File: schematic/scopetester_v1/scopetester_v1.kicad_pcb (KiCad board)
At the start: 2 copper layers, 73.7 x 54.4 mm, 42 parts, among them J1 CON_PWR, J2 Conn_01x04, J3 AVR_ISP, SW1 SW_Push, U1 ATmega8A-P, Y1 16MHz

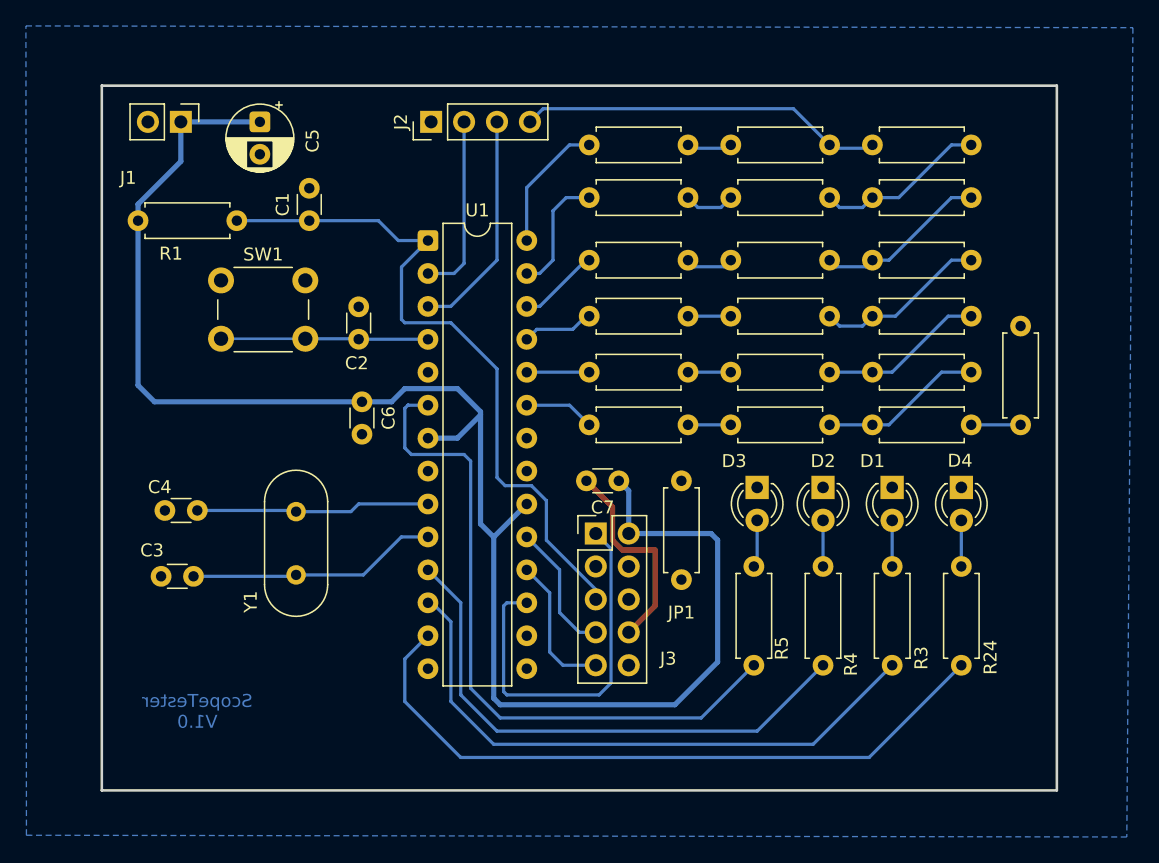
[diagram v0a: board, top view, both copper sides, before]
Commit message: Made tracks bit thicker & fixed few DRC warnings
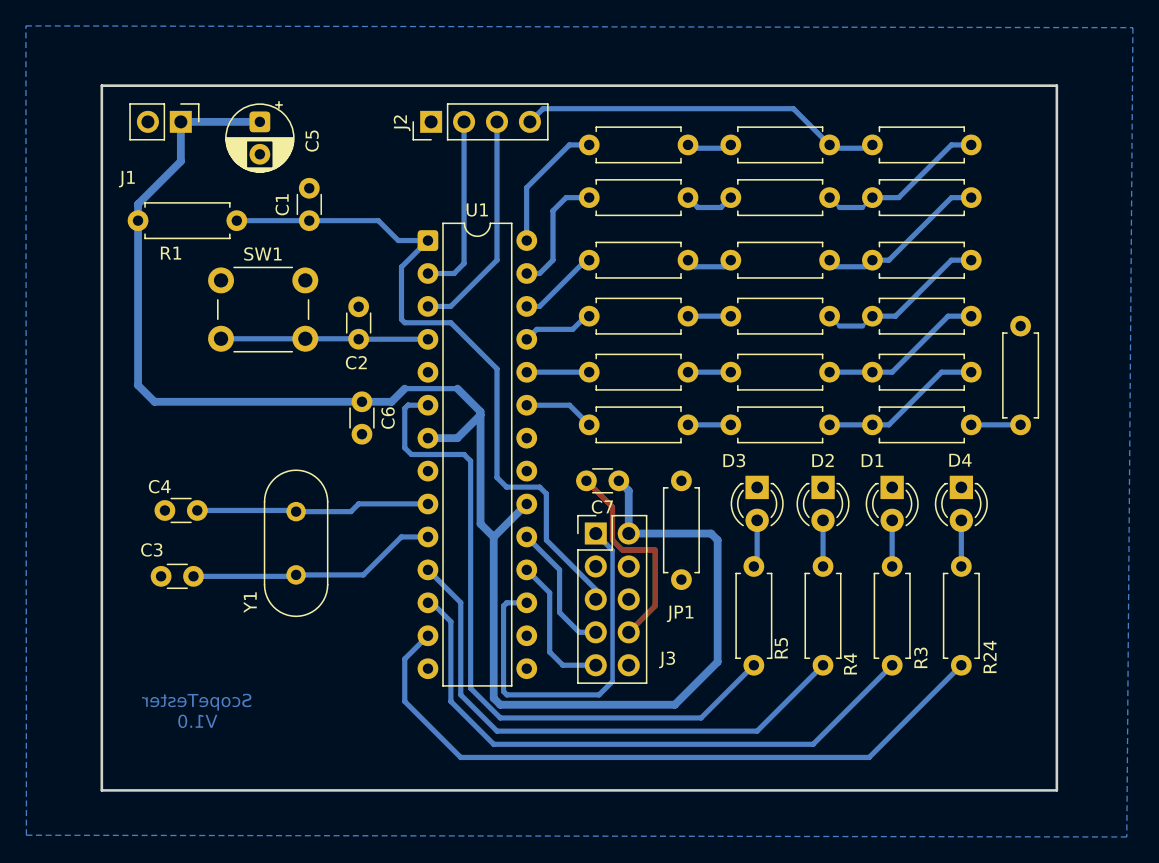
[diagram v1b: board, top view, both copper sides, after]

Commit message: Minor updates to PCB layout
Also includes:
* Cap C5 changes to 10uF from 1uF
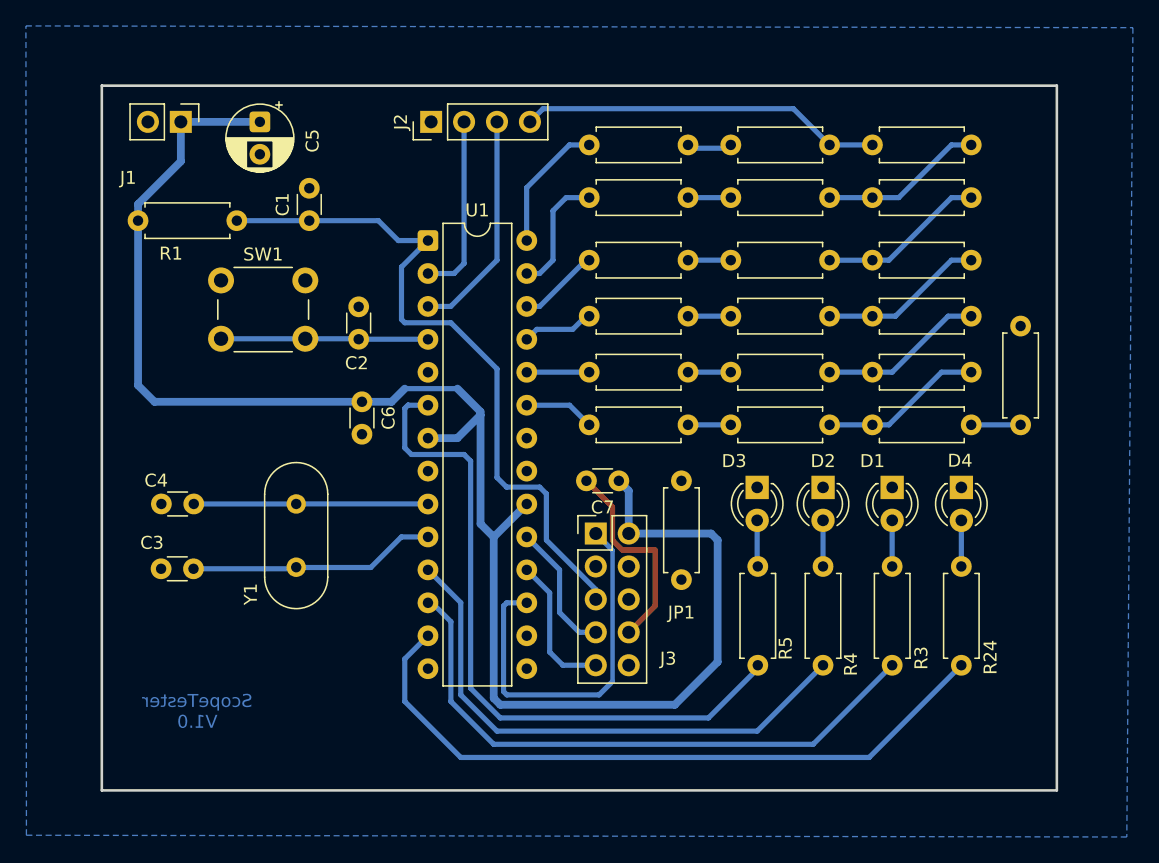
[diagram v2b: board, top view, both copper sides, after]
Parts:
- C5: value 1uF -> 10uF
- moved Y1 0.59 mm to (101.1, 91.7)
- moved C3 0.58 mm to (90.7, 96.7)
- moved C4 0.57 mm to (90.7, 91.7)
- moved R5 0.30 mm to (136.7, 96.5)
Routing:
- net Net-(R13-Pad2): track 13.3 -> 11.9 mm
- net Net-(R12-Pad1): track 3.93 -> 3.30 mm
- net Net-(R12-Pad2): track 13.2 -> 12.6 mm
- net Net-(R14-Pad2): track 13.3 -> 12.8 mm
- net ANG_OUT_0: track 27.5 -> 28.0 mm
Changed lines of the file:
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@@
 	(footprint "Resistor_THT:R_Axial_DIN0207_L6.3mm_D2.5mm_P7.62mm_Horizontal"
 		(layer "F.Cu")
-		(at 136.398 96.52 -90)
+		(at 136.7 96.52 -90)
 		(descr "Resistor, Axial_DIN0207 series, Axial, Horizontal, pin pitch=7.62mm, 0.25W = 1/4W, length*diameter=6.3*2.5mm^2, http://cdn-reichelt.de/documents/datenblatt/B400/1_4W%23YAG.pdf")
 		(tags "Resistor Axial_DIN0207 series Axial Horizontal pin pitch 7.62mm 0.25W = 1/4W length 6.3mm diameter 2.5mm")
@@
 	(footprint "Crystal:Crystal_HC49-4H_Vertical"
 		(layer "F.Cu")
-		(at 101.092 92.292 -90)
+		(at 101.1 91.7 -90)
 		(descr "HC-49-4H, Crystal, http://5hertz.com/pdfs/04404_D.pdf")
 		(property "Reference" "Y1"
@@
 			)
 		)
-		(property "Value" "1uF"
+		(property "Value" "10uF"
 			(at 1.205112 -5.334 90)
 			(layer "F.Fab")
@@
 	(footprint "Capacitor_THT:C_Disc_D3.0mm_W1.6mm_P2.50mm"
 		(layer "F.Cu")
-		(at 90.972 92.202)
+		(at 90.7 91.7)
 		(descr "C, Disc series, Radial, pin pitch=2.50mm, diameter*width=3.0*1.6mm^2, Capacitor, http://www.vishay.com/docs/45233/krseries.pdf")
 		(tags "C Disc series Radial pin pitch 2.50mm diameter 3.0mm width 1.6mm Capacitor")
@@
 	(footprint "Capacitor_THT:C_Disc_D3.0mm_W1.6mm_P2.50mm"
 		(layer "F.Cu")
-		(at 90.678 97.282)
+		(at 90.678 96.7)
 		(descr "C, Disc series, Radial, pin pitch=2.50mm, diameter*width=3.0*1.6mm^2, Capacitor, http://www.vishay.com/docs/45233/krseries.pdf")
 		(tags "C Disc series Radial pin pitch 2.50mm diameter 3.0mm width 1.6mm Capacitor")
@@
 	)
 	(segment
-		(start 109.21 94.244)
-		(end 111.262 94.244)
+		(start 93.178 96.7)
+		(end 100.98 96.7)
+		(width 0.4)
+		(layer "B.Cu")
+		(net 4)
+	)
+	(segment
+		(start 101.12 96.6)
+		(end 106.854 96.6)
 		(width 0.4)
 		(layer "B.Cu")
@@
 	)
 	(segment
-		(start 101.092 97.172)
-		(end 106.282 97.172)
+		(start 93.178 96.7)
+		(end 93.278 96.8)
 		(width 0.4)
 		(layer "B.Cu")
@@
 	)
 	(segment
-		(start 106.282 97.172)
+		(start 106.854 96.6)
 		(end 109.21 94.244)
 		(width 0.4)
@@
 	)
 	(segment
-		(start 93.178 97.282)
-		(end 100.982 97.282)
+		(start 100.98 96.7)
+		(end 101.1 96.58)
 		(width 0.4)
 		(layer "B.Cu")
@@
 	)
 	(segment
-		(start 93.472 92.202)
-		(end 101.002 92.202)
+		(start 101.1 96.58)
+		(end 101.12 96.6)
 		(width 0.4)
 		(layer "B.Cu")
-		(net 5)
+		(net 4)
 	)
 	(segment
-		(start 105.32 92.292)
-		(end 105.918 91.694)
+		(start 109.21 94.244)
+		(end 111.262 94.244)
 		(width 0.4)
 		(layer "B.Cu")
-		(net 5)
+		(net 4)
 	)
 	(segment
-		(start 101.092 92.292)
-		(end 105.32 92.292)
+		(start 101.1 91.7)
+		(end 101.106 91.694)
 		(width 0.4)
 		(layer "B.Cu")
@@
 	)
 	(segment
-		(start 105.918 91.694)
+		(start 101.106 91.694)
 		(end 111.252 91.694)
 		(width 0.4)
@@
 	)
 	(segment
+		(start 93.2 91.7)
+		(end 101.1 91.7)
+		(width 0.4)
+		(layer "B.Cu")
+		(net 5)
+	)
+	(segment
 		(start 147.066 96.52)
 		(end 147.066 92.964)
@@
 	)
 	(segment
-		(start 119.126 62.23)
-		(end 120.142 61.214)
+		(start 142.24 64.008)
+		(end 145.542 64.008)
 		(width 0.4)
 		(layer "B.Cu")
@@
 	)
 	(segment
-		(start 120.142 61.214)
-		(end 139.446 61.214)
+		(start 119.126 62.23)
+		(end 120.142 61.214)
 		(width 0.4)
 		(layer "B.Cu")
@@
 	)
 	(segment
-		(start 142.494 64.262)
-		(end 145.288 64.262)
+		(start 120.142 61.214)
+		(end 139.446 61.214)
 		(width 0.4)
 		(layer "B.Cu")
@@
 	)
 	(segment
-		(start 114.046 87.884)
-		(end 114.554 88.392)
+		(start 136.7 104.4)
+		(end 136.7 104.14)
 		(width 0.4)
 		(layer "B.Cu")
@@
 	)
 	(segment
-		(start 109.982 87.884)
-		(end 114.046 87.884)
+		(start 116.84 108.204)
+		(end 132.896 108.204)
 		(width 0.4)
 		(layer "B.Cu")
@@
 	)
 	(segment
-		(start 114.554 88.392)
-		(end 114.554 105.918)
+		(start 109.738 84.084)
+		(end 109.728 84.074)
 		(width 0.4)
 		(layer "B.Cu")
@@
 	)
 	(segment
-		(start 109.738 84.084)
-		(end 109.728 84.074)
+		(start 114.554 105.918)
+		(end 116.84 108.204)
 		(width 0.4)
 		(layer "B.Cu")
@@
 	)
 	(segment
-		(start 109.728 84.074)
-		(end 109.474 84.328)
+		(start 132.896 108.204)
+		(end 136.7 104.4)
 		(width 0.4)
 		(layer "B.Cu")
@@
 	)
 	(segment
-		(start 111.262 84.084)
-		(end 109.738 84.084)
+		(start 109.474 84.328)
+		(end 109.474 87.376)
 		(width 0.4)
 		(layer "B.Cu")
@@
 	)
 	(segment
-		(start 132.334 108.204)
-		(end 136.398 104.14)
+		(start 109.728 84.074)
+		(end 109.474 84.328)
 		(width 0.4)
 		(layer "B.Cu")
@@
 	)
 	(segment
-		(start 109.474 87.376)
-		(end 109.982 87.884)
+		(start 114.554 88.392)
+		(end 114.554 105.918)
 		(width 0.4)
 		(layer "B.Cu")
@@
 	)
 	(segment
-		(start 116.84 108.204)
-		(end 132.334 108.204)
+		(start 114.046 87.884)
+		(end 114.554 88.392)
 		(width 0.4)
 		(layer "B.Cu")
@@
 	)
 	(segment
-		(start 109.474 84.328)
-		(end 109.474 87.376)
+		(start 111.262 84.084)
+		(end 109.738 84.084)
 		(width 0.4)
 		(layer "B.Cu")
@@
 	)
 	(segment
-		(start 114.554 105.918)
-		(end 116.84 108.204)
+		(start 109.474 87.376)
+		(end 109.982 87.884)
+		(width 0.4)
+		(layer "B.Cu")
+		(net 18)
+	)
+	(segment
+		(start 109.982 87.884)
+		(end 114.046 87.884)
 		(width 0.4)
 		(layer "B.Cu")
@@
 	(segment
 		(start 131.318 72.898)
-		(end 131.826 73.406)
+		(end 131.302 72.898)
 		(width 0.4)
 		(layer "B.Cu")
@@
 	)
 	(segment
-		(start 131.826 73.406)
-		(end 134.112 73.406)
+		(start 131.302 72.898)
+		(end 134.62 72.898)
 		(width 0.4)
 		(layer "B.Cu")
@@
 	)
 	(segment
-		(start 134.112 73.406)
-		(end 134.62 72.898)
+		(start 131.302 72.898)
+		(end 131.3 72.9)
 		(width 0.4)
 		(layer "B.Cu")
@@
 	)
 	(segment
-		(start 143.002 68.834)
-		(end 144.78 68.834)
+		(start 151.638 64.008)
+		(end 147.574 68.072)
 		(width 0.4)
 		(layer "B.Cu")
@@
 	)
 	(segment
-		(start 151.638 64.008)
-		(end 147.574 68.072)
+		(start 153.162 64.008)
+		(end 151.638 64.008)
 		(width 0.4)
 		(layer "B.Cu")
@@
 	)
 	(segment
-		(start 153.162 64.008)
-		(end 151.638 64.008)
+		(start 142.24 68.072)
+		(end 142.272 68.072)
 		(width 0.4)
 		(layer "B.Cu")
@@
 	)
 	(segment
-		(start 144.78 68.834)
-		(end 145.542 68.072)
-		(width 0.25)
+		(start 142.3 68.1)
+		(end 142.328 68.072)
+		(width 0.4)
 		(layer "B.Cu")
 		(net 27)
 	)
 	(segment
-		(start 142.24 68.072)
-		(end 143.002 68.834)
-		(width 0.25)
+		(start 142.272 68.072)
+		(end 142.3 68.1)
+		(width 0.4)
 		(layer "B.Cu")
 		(net 27)
@@
 	)
 	(segment
-		(start 147.32 77.216)
-		(end 145.542 77.216)
+		(start 142.328 68.072)
+		(end 145.542 68.072)
 		(width 0.4)
 		(layer "B.Cu")
+		(net 27)
+	)
+	(segment
+		(start 142.24 77.24)
+		(end 142.3 77.3)
+		(width 0.2)
+		(layer "F.Cu")
 		(net 28)
 	)
 	(segment
-		(start 153.162 72.898)
-		(end 151.638 72.898)
-		(width 0.4)
-		(layer "B.Cu")
+		(start 142.24 77.216)
+		(end 142.24 77.24)
+		(width 0.2)
+		(layer "F.Cu")
 		(net 28)
 	)
 	(segment
-		(start 143.002 77.978)
-		(end 144.78 77.978)
+		(start 147.32 77.216)
+		(end 145.542 77.216)
 		(width 0.4)
 		(layer "B.Cu")
@@
 	)
 	(segment
-		(start 142.24 77.216)
-		(end 143.002 77.978)
-		(width 0.25)
+		(start 153.162 72.898)
+		(end 151.638 72.898)
+		(width 0.4)
 		(layer "B.Cu")
 		(net 28)
@@
 	)
 	(segment
-		(start 144.78 77.978)
+		(start 142.24 77.216)
 		(end 145.542 77.216)
-		(width 0.25)
+		(width 0.4)
 		(layer "B.Cu")
 		(net 28)
@@
 	(segment
 		(start 131.318 68.072)
-		(end 132.08 68.834)
-		(width 0.4)
-		(layer "B.Cu")
-		(net 43)
-	)
-	(segment
-		(start 132.08 68.834)
-		(end 133.858 68.834)
-		(width 0.4)
-		(layer "B.Cu")
-		(net 43)
-	)
-	(segment
-		(start 133.858 68.834)
 		(end 134.62 68.072)
 		(width 0.4)
@@
 	)
 	(segment
-		(start 142.748 73.406)
-		(end 145.034 73.406)
+		(start 142.657 72.9)
+		(end 144.943 72.9)
 		(width 0.4)
 		(layer "B.Cu")
@@
 		(layer "B.Cu")
 		(net 45)
-	)
-	(segment
-		(start 142.24 72.898)
-		(end 142.748 73.406)
-		(width 0.25)
-		(layer "B.Cu")
-		(net 45)
-	)
-	(segment
-		(start 145.034 73.406)
-		(end 145.542 72.898)
-		(width 0.25)
-		(layer "B.Cu")
-		(net 45)

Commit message: PCB changes to make layout less dense
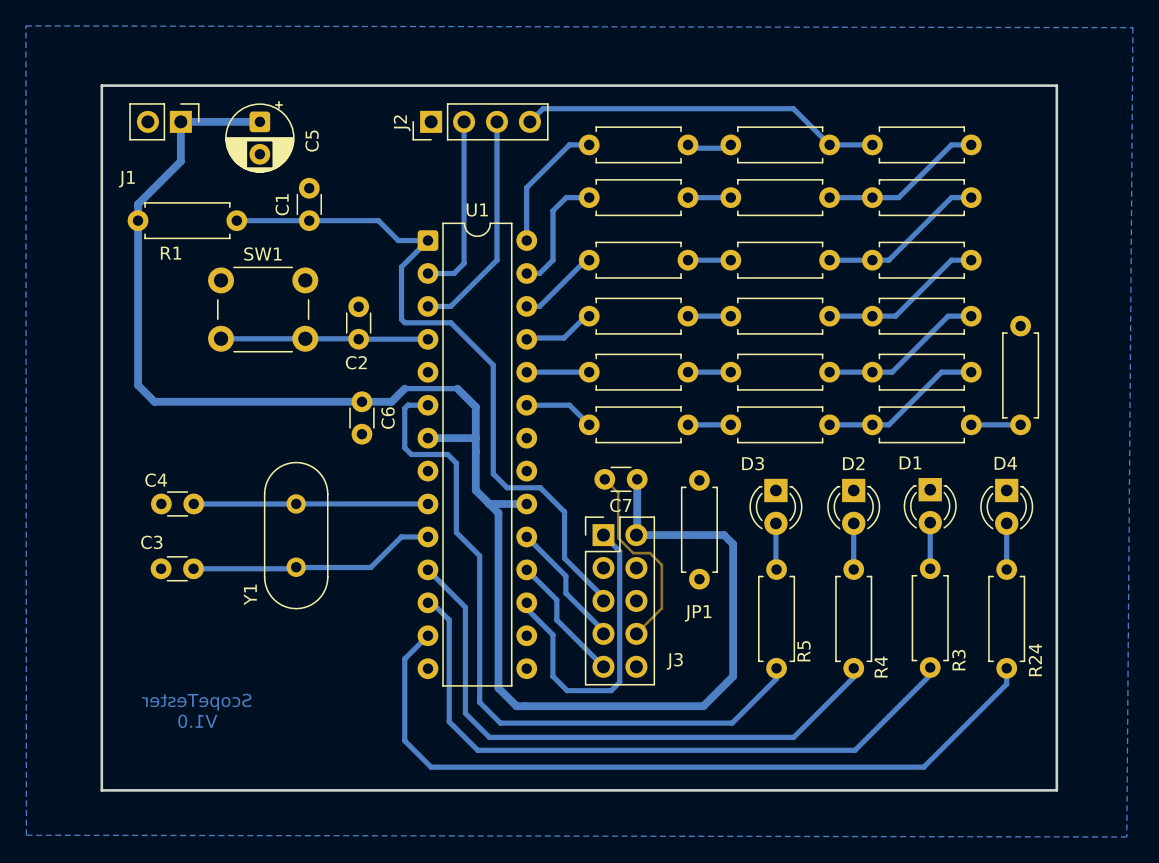
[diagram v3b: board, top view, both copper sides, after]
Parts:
- moved R24 3.51 mm to (155.9, 96.8)
- moved D4 3.51 mm to (155.9, 90.7)
- moved R3 2.94 mm to (150.0, 96.7)
- moved D1 2.94 mm to (150.0, 90.6)
- moved R4 2.38 mm to (144.1, 96.8)
- moved D2 2.38 mm to (144.1, 90.7)
- moved R5 1.47 mm to (138.1, 96.8)
- moved D3 1.47 mm to (138.1, 90.7)
- moved C7 1.42 mm to (127.4, 89.8)
- moved JP1 1.39 mm to (132.2, 97.5)
- moved J3 0.61 mm to (124.8, 94.1)
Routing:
- net STAT_LED_3: track 53.5 -> 60.0 mm
- net ISP_MOSI: track 29.4 -> 24.3 mm
- net STAT_LED_2: track 46.1 -> 50.7 mm
- net STAT_LED_1: track 41.9 -> 45.6 mm
- net STAT_LED_0: track 52.9 -> 54.4 mm
- net ISP_MISO: track 11.0 -> 9.93 mm
- net GND: track 16.2 -> 15.3 mm

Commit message: Minor changes, project name & version update
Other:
- board text added: "signal.echo V1.1"
- board text removed: "ScopeTester V1.0"
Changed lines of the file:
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@@
 		(layer "Edge.Cuts")
 	)
-	(gr_text "ScopeTester\nV1.0"
+	(gr_text "signal.echo\nV1.1"
 		(at 93.472 107.696 0)
 		(layer "B.Cu")
@@
 	)
 	(segment
-		(start 93.178 96.7)
-		(end 93.278 96.8)
-		(width 0.4)
-		(layer "B.Cu")
-		(net 4)
-	)
-	(segment
 		(start 106.854 96.6)
 		(end 109.21 94.244)
@@
 	)
 	(segment
-		(start 124.8 101.72)
-		(end 124.8 101.485)
+		(start 118.882 94.244)
+		(end 121.9 97.262)
 		(width 0.4)
 		(layer "B.Cu")
@@
 	)
 	(segment
-		(start 121.9 98.585)
-		(end 121.9 97.262)
+		(start 121.9 98.82)
+		(end 124.8 101.72)
 		(width 0.4)
 		(layer "B.Cu")
@@
 	(segment
 		(start 121.9 97.262)
-		(end 118.882 94.244)
+		(end 121.9 98.82)
 		(width 0.4)
 		(layer "B.Cu")
@@
 	)
 	(segment
-		(start 124.8 101.485)
-		(end 121.9 98.585)
-		(width 0.4)
-		(layer "B.Cu")
-		(net 13)
-	)
-	(segment
-		(start 124.8 104.25)
-		(end 121.2 100.65)
+		(start 118.882 96.784)
+		(end 121.2 99.102)
 		(width 0.4)
 		(layer "B.Cu")
@@
 	(segment
 		(start 121.2 99.102)
-		(end 118.882 96.784)
+		(end 121.2 100.73)
 		(width 0.4)
 		(layer "B.Cu")
@@
 	)
 	(segment
-		(start 124.8 104.26)
-		(end 124.8 104.25)
+		(start 121.2 100.73)
+		(end 124.73 104.26)
 		(width 0.4)
 		(layer "B.Cu")
@@
 	)
 	(segment
-		(start 121.2 100.65)
-		(end 121.2 99.102)
+		(start 124.73 104.26)
+		(end 124.8 104.26)
 		(width 0.4)
 		(layer "B.Cu")
@@
 	)
 	(segment
-		(start 120.904 69.088)
+		(start 121.1 68.892)
 		(end 121.92 68.072)
-		(width 0.4)
-		(layer "B.Cu")
-		(net 19)
-	)
-	(segment
-		(start 120.904 72.898)
-		(end 120.904 69.088)
-		(width 0.4)
-		(layer "B.Cu")
-		(net 19)
-	)
-	(segment
-		(start 118.882 73.924)
-		(end 119.878 73.924)
 		(width 0.4)
 		(layer "B.Cu")
@@
 	)
 	(segment
-		(start 119.878 73.924)
-		(end 120.904 72.898)
+		(start 120.226 73.924)
+		(end 121.1 73.05)
 		(width 0.4)
 		(layer "B.Cu")
@@
 	)
 	(segment
-		(start 119.878 76.464)
+		(start 118.882 73.924)
+		(end 120.226 73.924)
+		(width 0.4)
+		(layer "B.Cu")
+		(net 19)
+	)
+	(segment
+		(start 121.1 73.05)
+		(end 121.1 68.892)
+		(width 0.4)
+		(layer "B.Cu")
+		(net 19)
+	)
+	(segment
+		(start 120.336 76.464)
+		(end 123.444 73.356)
+		(width 0.4)
+		(layer "B.Cu")
+		(net 20)
+	)
+	(segment
+		(start 123.444 73.356)
 		(end 123.444 72.898)
 		(width 0.4)
@@
 	(segment
 		(start 118.882 76.464)
-		(end 119.878 76.464)
+		(end 120.336 76.464)
 		(width 0.4)
 		(layer "B.Cu")
@@
 	)
 	(segment
-		(start 131.302 72.898)
-		(end 131.3 72.9)
-		(width 0.4)
-		(layer "B.Cu")
-		(net 21)
-	)
-	(segment
 		(start 121.76 78.9)
 		(end 123.444 77.216)
@@
 	)
 	(segment
-		(start 142.24 77.24)
-		(end 142.3 77.3)
-		(width 0.2)
-		(layer "F.Cu")
-		(net 28)
-	)
-	(segment
-		(start 142.24 77.216)
-		(end 142.24 77.24)
-		(width 0.2)
-		(layer "F.Cu")
-		(net 28)
-	)
-	(segment
 		(start 147.32 77.216)
 		(end 145.542 77.216)
@@
 	(segment
 		(start 118.1 107.3)
-		(end 118.75 107.3)
+		(end 132.5 107.3)
 		(width 0.6)
 		(layer "B.Cu")
@@
 	(segment
 		(start 114.95 86.6)
-		(end 114.95 87.65)
-		(width 0.6)
-		(layer "B.Cu")
-		(net 32)
-	)
-	(segment
-		(start 118.75 107.3)
-		(end 132.5 107.3)
+		(end 114.95 90.65)
 		(width 0.6)
 		(layer "B.Cu")
@@
 		(width 0.6)
 		(layer "B.Cu")
-		(net 32)
-	)
-	(segment
-		(start 114.95 90.65)
-		(end 114.95 87.65)
-		(width 0.6)
-		(layer "B.Cu")
